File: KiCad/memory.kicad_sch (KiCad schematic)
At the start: 7 parts, among them U1001 IS25LP032D-JNLE, U1002 APS6404

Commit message: Combo-Footprint für Flash (auch im Schematic)
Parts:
- U1001: footprint Package_SO:SOIC-8_3.9x4.9mm_P1.27mm -> Library:SOIC-8_4_5.3_combo_P1.27mm
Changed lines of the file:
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@@
 			)
 		)
-		(property "Footprint" "Package_SO:SOIC-8_3.9x4.9mm_P1.27mm"
+		(property "Footprint" "Library:SOIC-8_4_5.3_combo_P1.27mm"
 			(at 209.55 72.39 0)
 			(effects

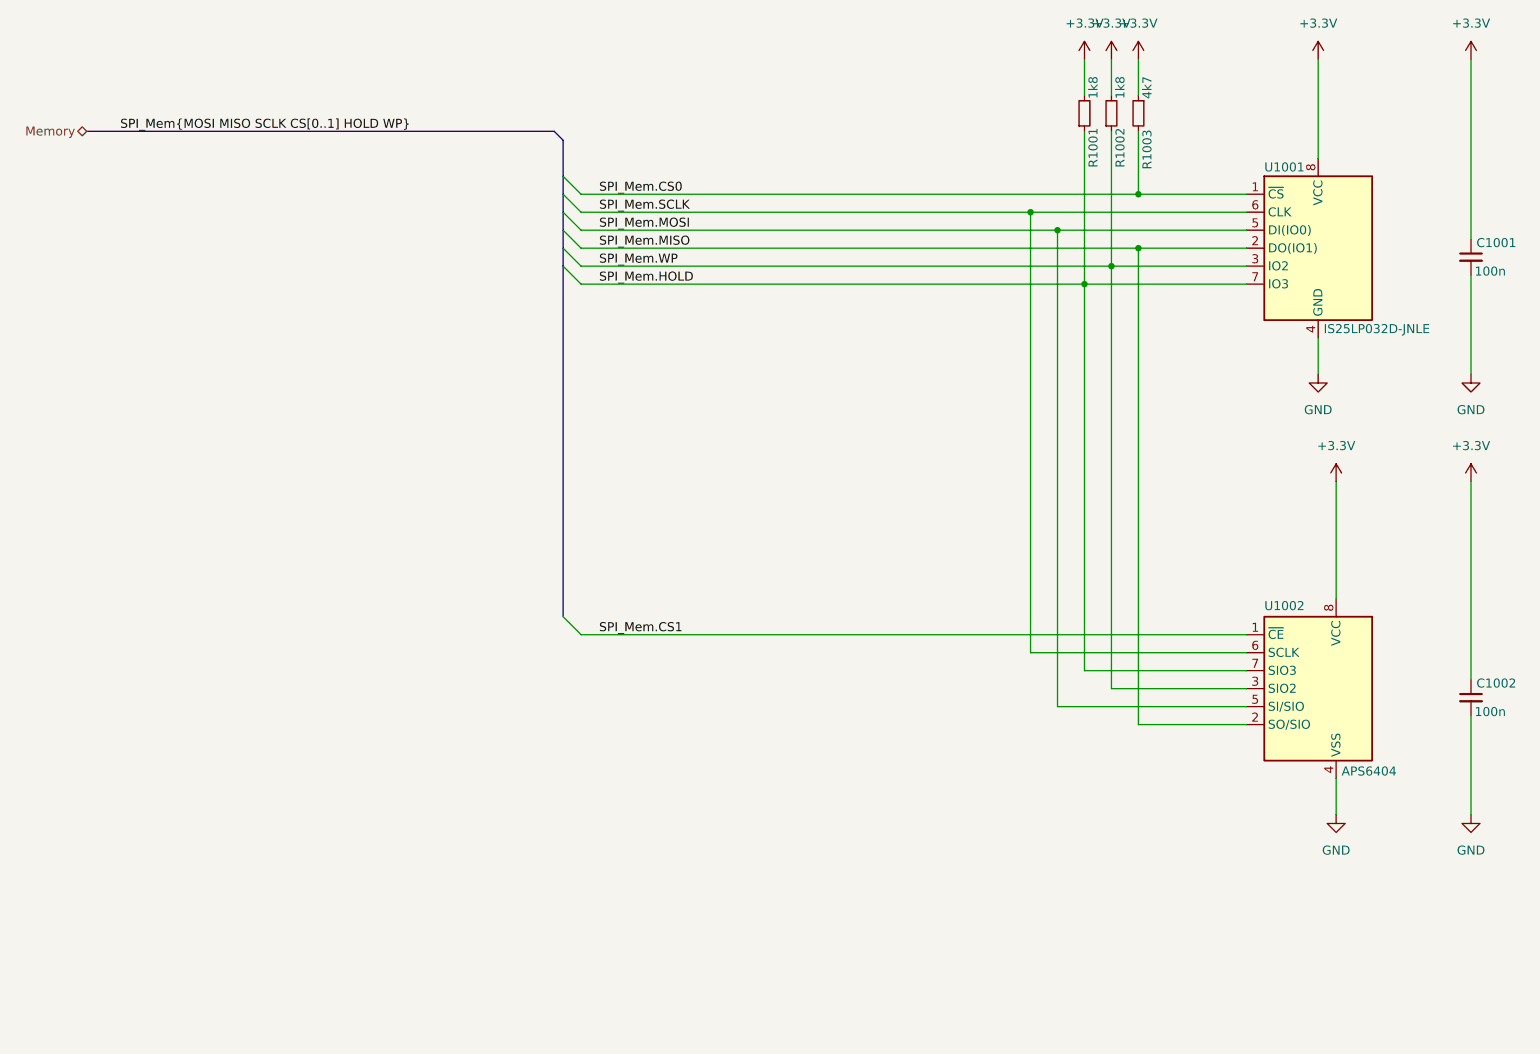
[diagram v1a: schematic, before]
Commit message: micro-SD hinzugefügt
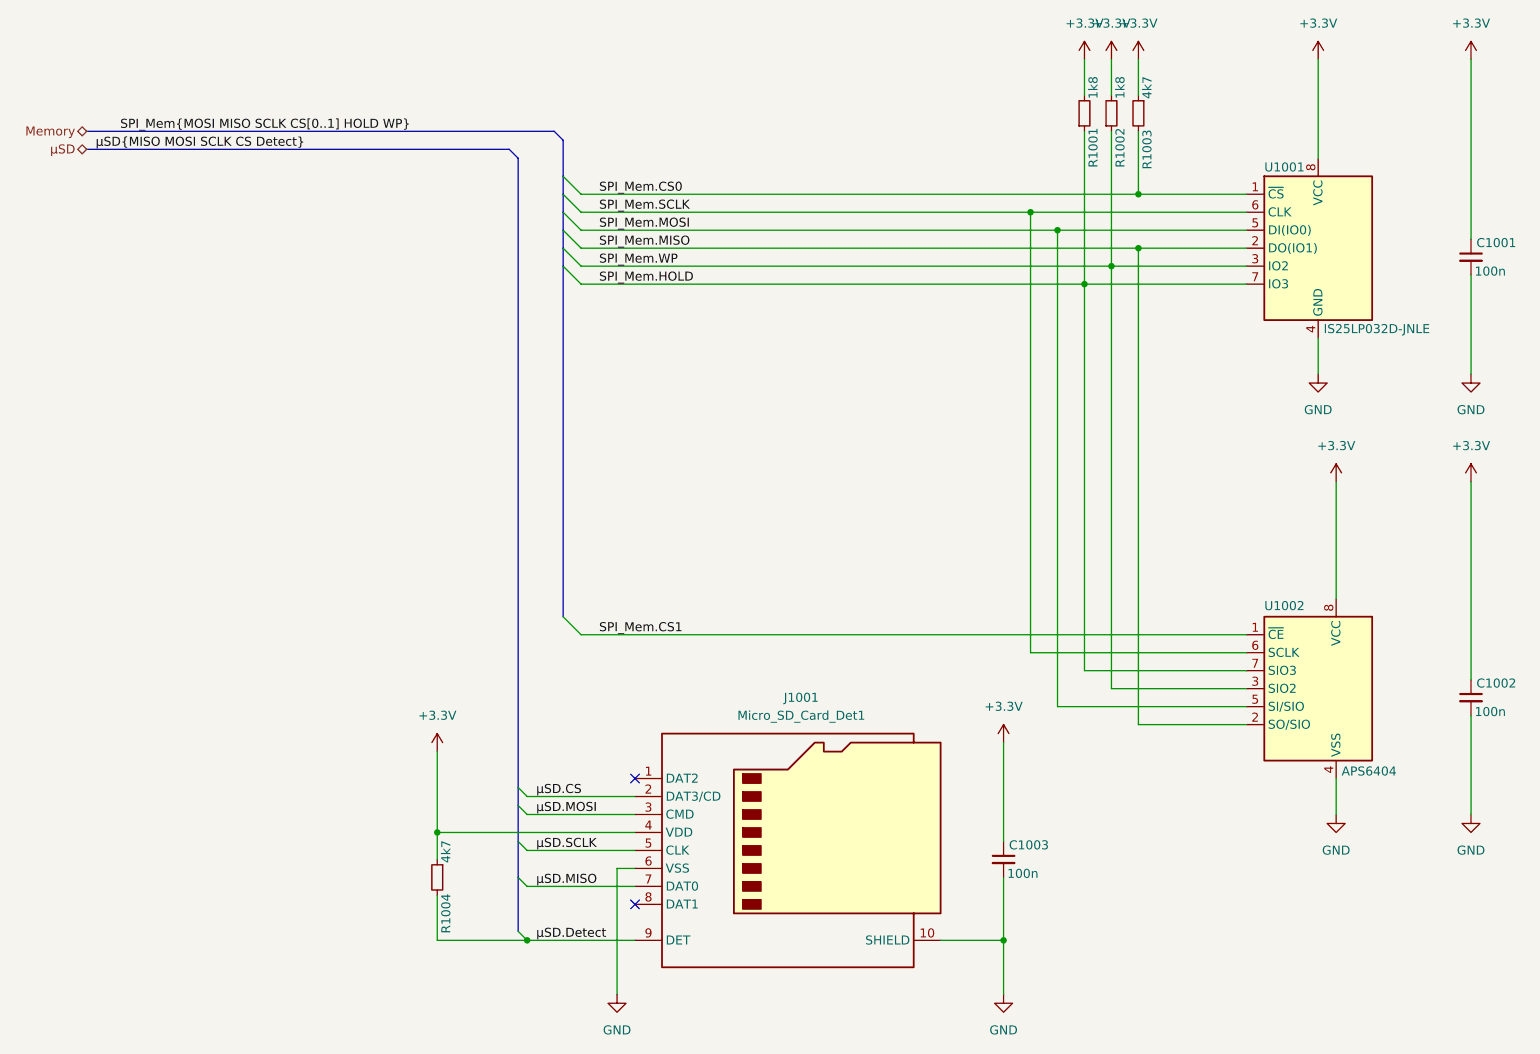
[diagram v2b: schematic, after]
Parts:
- added C1003: 100n, Capacitor_SMD:C_0402_1005Metric, symbol Device:C_Small
- added J1001: Micro_SD_Card_Det1, Library:microSD_Wuerth_693071010811, symbol Connector:Micro_SD_Card_Det1
- added R1004: 4k7, Resistor_SMD:R_0402_1005Metric, symbol Device:R_Small
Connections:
- net +3.3V: now also C1003.1, J1001.4 (VDD), R1004.1
- net GND: now also C1003.2, J1001.10 (SHIELD), J1001.6 (VSS)
- new net μSD.CS: J1001.2 (DAT3/CD)
- new net μSD.Detect: J1001.9 (DET), R1004.2
- new net μSD.MISO: J1001.7 (DAT0)
- new net μSD.MOSI: J1001.3 (CMD)
- new net μSD.SCLK: J1001.5 (CLK)
- no-connect marks 0 -> 2

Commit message: LEDs zur Visualisierung des ausgewählten FPGAs
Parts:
- R1004: value 4k7 -> 10k; Würth 560112110245 -> 560112110020
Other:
- moved on the sheet: R1001, R1002
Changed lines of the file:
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@@
 	)
 	(junction
-		(at 176.53 77.47)
+		(at 172.72 77.47)
 		(diameter 0)
 		(color 0 0 0 0)
@@
 	)
 	(junction
-		(at 172.72 69.85)
+		(at 180.34 69.85)
 		(diameter 0)
 		(color 0 0 0 0)
@@
 	)
 	(junction
-		(at 180.34 74.93)
+		(at 176.53 74.93)
 		(diameter 0)
 		(color 0 0 0 0)
@@
 	(wire
 		(pts
-			(xy 176.53 55.88) (xy 176.53 77.47)
-		)
-		(stroke
-			(width 0)
-			(type default)
-		)
-	)
-	(wire
-		(pts
-			(xy 180.34 134.62) (xy 199.39 134.62)
-		)
-		(stroke
-			(width 0)
-			(type default)
-		)
-	)
-	(wire
-		(pts
-			(xy 176.53 132.08) (xy 176.53 77.47)
+			(xy 172.72 55.88) (xy 172.72 77.47)
+		)
+		(stroke
+			(width 0)
+			(type default)
+		)
+	)
+	(wire
+		(pts
+			(xy 176.53 134.62) (xy 199.39 134.62)
+		)
+		(stroke
+			(width 0)
+			(type default)
+		)
+	)
+	(wire
+		(pts
+			(xy 172.72 132.08) (xy 172.72 77.47)
 		)
 		(stroke
@@
 	(wire
 		(pts
-			(xy 176.53 77.47) (xy 199.39 77.47)
+			(xy 172.72 77.47) (xy 199.39 77.47)
 		)
 		(stroke
@@
 	(wire
 		(pts
-			(xy 172.72 137.16) (xy 199.39 137.16)
+			(xy 180.34 137.16) (xy 199.39 137.16)
 		)
 		(stroke
@@
 	(wire
 		(pts
-			(xy 176.53 132.08) (xy 199.39 132.08)
-		)
-		(stroke
-			(width 0)
-			(type default)
-		)
-	)
-	(wire
-		(pts
-			(xy 199.39 69.85) (xy 172.72 69.85)
+			(xy 172.72 132.08) (xy 199.39 132.08)
 		)
 		(stroke
@@
 	(wire
 		(pts
-			(xy 180.34 134.62) (xy 180.34 74.93)
+			(xy 176.53 134.62) (xy 176.53 74.93)
 		)
 		(stroke
@@
 	(wire
 		(pts
-			(xy 105.41 69.85) (xy 172.72 69.85)
+			(xy 105.41 69.85) (xy 180.34 69.85)
 		)
 		(stroke
@@
 	(wire
 		(pts
-			(xy 172.72 137.16) (xy 172.72 69.85)
-		)
-		(stroke
-			(width 0)
-			(type default)
-		)
-	)
-	(wire
-		(pts
-			(xy 105.41 74.93) (xy 180.34 74.93)
+			(xy 180.34 137.16) (xy 180.34 69.85)
+		)
+		(stroke
+			(width 0)
+			(type default)
+		)
+	)
+	(wire
+		(pts
+			(xy 105.41 74.93) (xy 176.53 74.93)
 		)
 		(stroke
@@
 	(wire
 		(pts
-			(xy 180.34 45.72) (xy 180.34 50.8)
-		)
-		(stroke
-			(width 0)
-			(type default)
-		)
-	)
-	(wire
-		(pts
-			(xy 180.34 74.93) (xy 199.39 74.93)
+			(xy 176.53 45.72) (xy 176.53 50.8)
+		)
+		(stroke
+			(width 0)
+			(type default)
+		)
+	)
+	(wire
+		(pts
+			(xy 176.53 74.93) (xy 199.39 74.93)
 		)
 		(stroke
@@
 	(wire
 		(pts
-			(xy 180.34 55.88) (xy 180.34 74.93)
+			(xy 176.53 55.88) (xy 176.53 74.93)
 		)
 		(stroke
@@
 	(wire
 		(pts
-			(xy 105.41 77.47) (xy 176.53 77.47)
+			(xy 105.41 77.47) (xy 172.72 77.47)
+		)
+		(stroke
+			(width 0)
+			(type default)
+		)
+	)
+	(wire
+		(pts
+			(xy 180.34 69.85) (xy 199.39 69.85)
 		)
 		(stroke
@@
 	(wire
 		(pts
-			(xy 176.53 45.72) (xy 176.53 50.8)
+			(xy 172.72 45.72) (xy 172.72 50.8)
 		)
 		(stroke
@@
 			)
 		)
-		(property "Value" "4k7"
+		(property "Value" "10k"
 			(at 85.598 159.258 90)
 			(show_name no)
@@
 			)
 		)
-		(property "Würth" "560112110245"
+		(property "Würth" "560112110020"
 			(at 85.09 161.29 0)
 			(hide yes)
@@
 	(symbol
 		(lib_id "Device:R_Small")
-		(at 180.34 53.34 0)
+		(at 176.53 53.34 0)
 		(mirror x)
 		(unit 1)
@@
 		(dnp no)
 		(property "Reference" "R1002"
-			(at 180.848 55.372 90)
+			(at 177.038 55.372 90)
 			(show_name no)
 			(do_not_autoplace no)
@@
 		)
 		(property "Value" "1k8"
-			(at 180.848 51.308 90)
+			(at 177.038 51.308 90)
 			(show_name no)
 			(do_not_autoplace no)
@@
 		)
 		(property "Footprint" "Resistor_SMD:R_0402_1005Metric"
-			(at 180.34 53.34 0)
+			(at 176.53 53.34 0)
 			(hide yes)
 			(show_name no)
@@
 		)
 		(property "Datasheet" ""
-			(at 180.34 53.34 0)
+			(at 176.53 53.34 0)
 			(hide yes)
 			(show_name no)
@@
 		)
 		(property "Description" "Resistor, small symbol"
-			(at 180.34 53.34 0)
+			(at 176.53 53.34 0)
 			(hide yes)
 			(show_name no)
@@
 		)
 		(property "Würth" "560112110209"
-			(at 180.34 53.34 0)
+			(at 176.53 53.34 0)
 			(hide yes)
 			(show_name no)
@@
 	(symbol
 		(lib_id "Device:R_Small")
-		(at 176.53 53.34 0)
+		(at 172.72 53.34 0)
 		(mirror x)
 		(unit 1)
@@
 		(dnp no)
 		(property "Reference" "R1001"
-			(at 177.038 55.372 90)
+			(at 173.228 55.372 90)
 			(show_name no)
 			(do_not_autoplace no)
@@
 		)
 		(property "Value" "1k8"
-			(at 177.038 51.308 90)
+			(at 173.228 51.308 90)
 			(show_name no)
 			(do_not_autoplace no)
@@
 		)
 		(property "Footprint" "Resistor_SMD:R_0402_1005Metric"
-			(at 176.53 53.34 0)
+			(at 172.72 53.34 0)
 			(hide yes)
 			(show_name no)
@@
 		)
 		(property "Datasheet" ""
-			(at 176.53 53.34 0)
+			(at 172.72 53.34 0)
 			(hide yes)
 			(show_name no)
@@
 		)
 		(property "Description" "Resistor, small symbol"
-			(at 176.53 53.34 0)
+			(at 172.72 53.34 0)
 			(hide yes)
 			(show_name no)
@@
 		)
 		(property "Würth" "560112110209"
-			(at 176.53 53.34 0)
+			(at 172.72 53.34 0)
 			(hide yes)
 			(show_name no)
@@
 	(symbol
 		(lib_id "power:+3.3V")
-		(at 176.53 45.72 0)
+		(at 172.72 45.72 0)
 		(mirror y)
 		(unit 1)
@@
 		(dnp no)
 		(property "Reference" "#PWR01001"
-			(at 176.53 49.53 0)
+			(at 172.72 49.53 0)
 			(hide yes)
 			(show_name no)
@@
 		)
 		(property "Value" "+3.3V"
-			(at 176.53 40.64 0)
+			(at 172.72 40.64 0)
 			(show_name no)
 			(do_not_autoplace no)
@@
 		)
 		(property "Footprint" ""
-			(at 176.53 45.72 0)
+			(at 172.72 45.72 0)
 			(hide yes)
 			(show_name no)
@@
 		)
 		(property "Datasheet" ""
-			(at 176.53 45.72 0)
+			(at 172.72 45.72 0)
 			(hide yes)
 			(show_name no)
@@
 		)
 		(property "Description" "Power symbol creates a global label with name \"+3.3V\""
-			(at 176.53 45.72 0)
+			(at 172.72 45.72 0)
 			(hide yes)
 			(show_name no)
@@
 	(symbol
 		(lib_id "power:+3.3V")
-		(at 180.34 45.72 0)
+		(at 176.53 45.72 0)
 		(mirror y)
 		(unit 1)
@@
 		(dnp no)
 		(property "Reference" "#PWR01002"
-			(at 180.34 49.53 0)
+			(at 176.53 49.53 0)
 			(hide yes)
 			(show_name no)
@@
 		)
 		(property "Value" "+3.3V"
-			(at 180.34 40.64 0)
+			(at 176.53 40.64 0)
 			(show_name no)
 			(do_not_autoplace no)
@@
 		)
 		(property "Footprint" ""
-			(at 180.34 45.72 0)
+			(at 176.53 45.72 0)
 			(hide yes)
 			(show_name no)
@@
 		)
 		(property "Datasheet" ""
-			(at 180.34 45.72 0)
+			(at 176.53 45.72 0)
 			(hide yes)
 			(show_name no)
@@
 		)
 		(property "Description" "Power symbol creates a global label with name \"+3.3V\""
-			(at 180.34 45.72 0)
-			(hide yes)
-			(show_name no)
+			(at 176.53 45.72 0)
+			(hide yes)
+			(show_name no)
